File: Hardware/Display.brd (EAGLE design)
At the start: 48 x 70 mm, 54 parts, among them IC1 STM32F030C6T, IC2 VREG-TS1117CW-3V3, M1 WIRELESS-NRF24L01, Q1 BSS138, Q10 BSS138, Q11 IRLML5203, Q12 BSS138, Q13 IRLML5203, Q14 BSS138, Q15 IRLML5203, Q16 BSS138, Q2 BSS138, Q3 BSS138, Q4 BSS138, Q5 BSS138, Q6 BSS138, Q7 BSS138, Q8 BSS138, Q9 IRLML5203

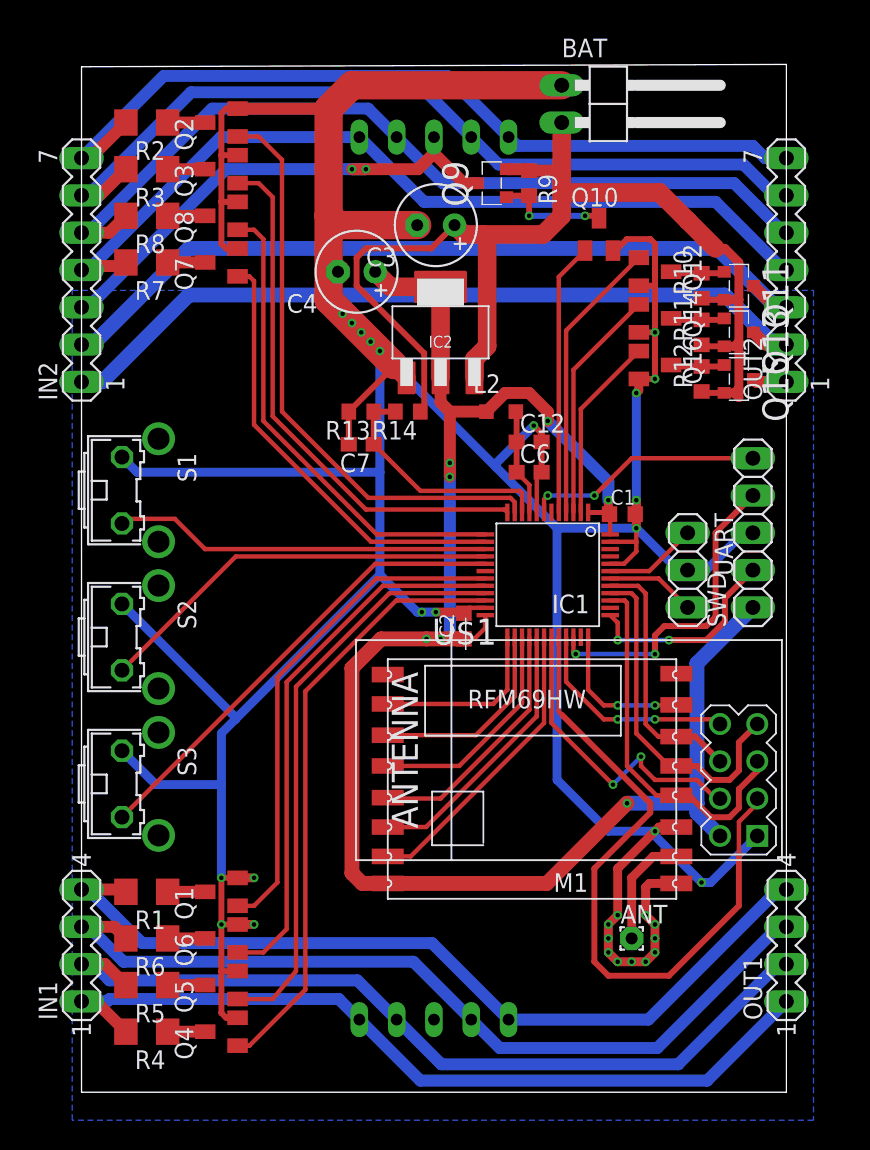
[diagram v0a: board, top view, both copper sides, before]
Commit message: Further software (Switches, HAL)
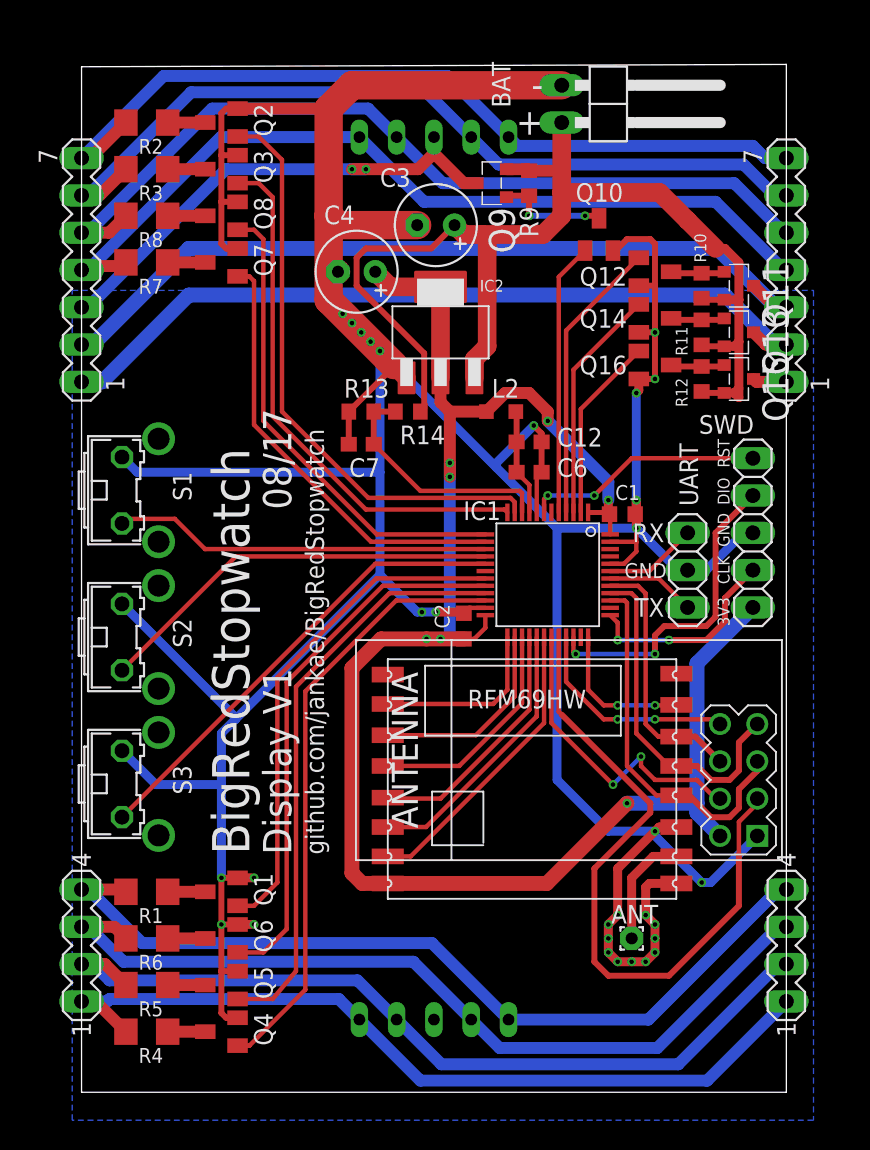
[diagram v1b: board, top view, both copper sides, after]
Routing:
- net GND: track 310.5 -> 312.4 mm
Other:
- board text added: "+"
- board text added: "-"
- board text added: "08/17"
- board text added: "3V3"
- board text added: "BigRedStopwatch"
- board text added: "CLK"
- board text added: "DIO"
- board text added: "Display V1"
- board text added: "GND"
- board text added: "RST"
- board text added: "RX"
- board text added: "TX"
- board text added: "github.com/jankae/BigRedStopwatch"

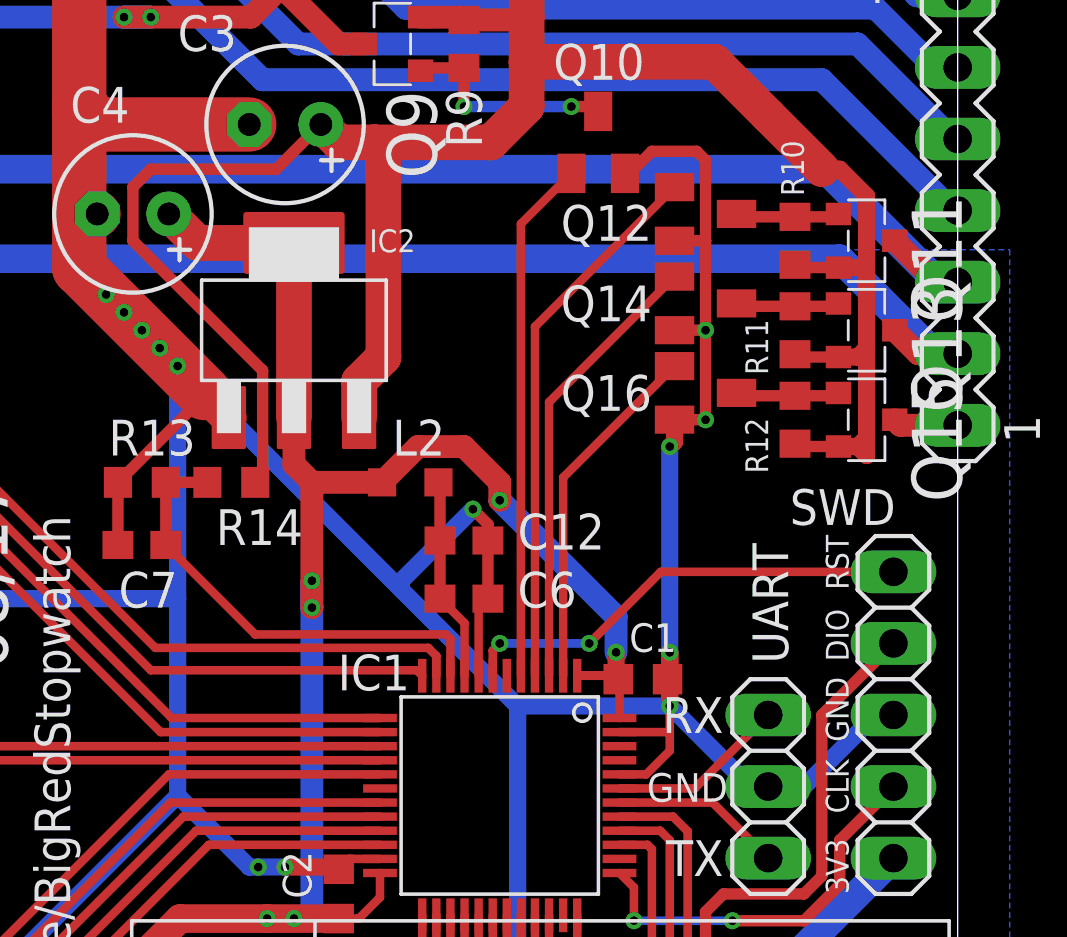
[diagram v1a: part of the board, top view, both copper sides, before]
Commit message: Added crystal to display board
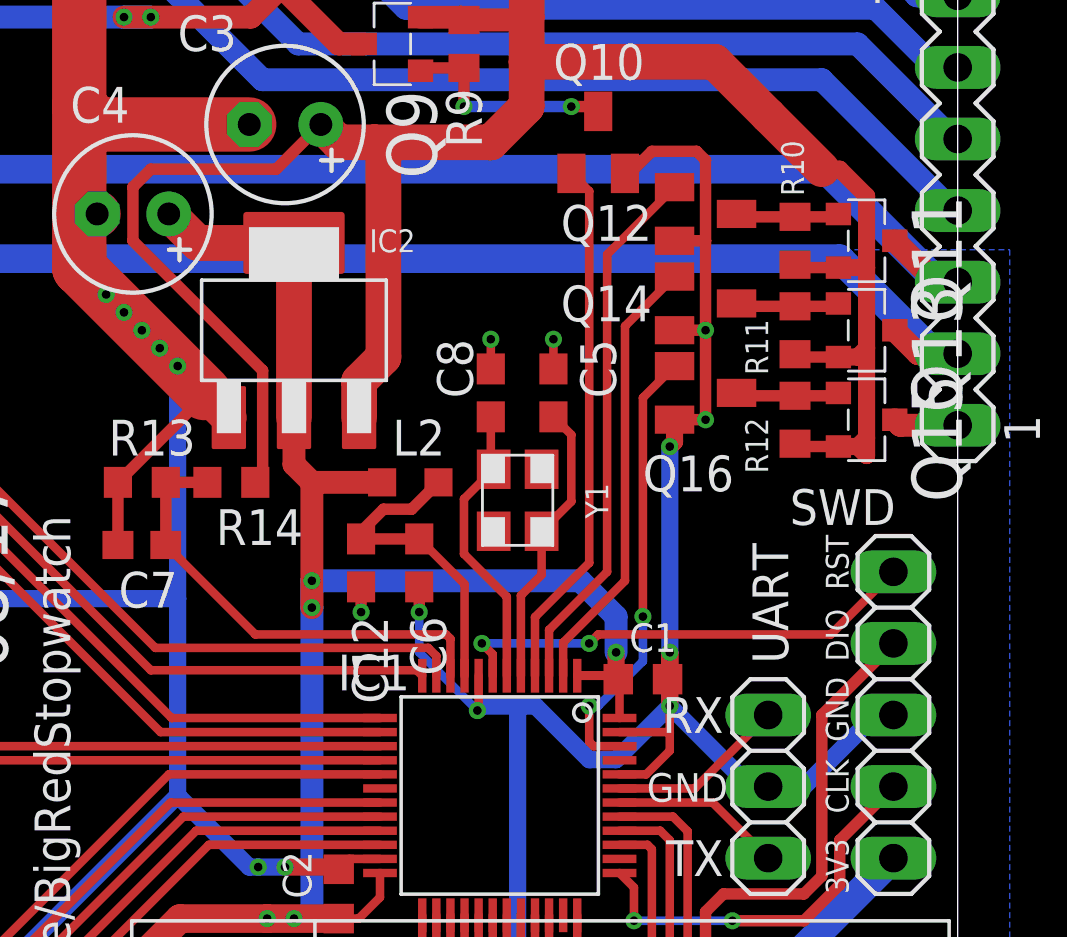
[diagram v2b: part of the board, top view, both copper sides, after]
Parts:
- added C5, C8: 12p, rcl:C0603
- added Y1: 8MHz, abracon:3.2X2.5MM
- moved C12 3.74 mm to (26.8, 43.5), turned to 270 degrees
- moved C6 2.03 mm to (28.9, 43.5), turned to 270 degrees
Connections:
- new net N$15: C5.2, IC1.5, Y1.3
- new net N$19: C8.2, IC1.6, Y1.1
- net DIGIT1: now also IC1.4; no longer IC1.5
- net DIGIT2: now also IC1.3; no longer IC1.4
- net DIGIT3: now also IC1.2; no longer IC1.3
- net DIGIT4: now also IC1.46; no longer IC1.2
- net GND: now also C5.1, C8.1
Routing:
- net GND: track 312.4 -> 297.7 mm, vias 30 -> 34
- net N$19: track 0.00 -> 10.3 mm
- net N$15: track 0.00 -> 10.2 mm
- net N$13: track 7.25 -> 11.4 mm
- net DIGIT4: track 12.6 -> 15.9 mm, vias 0 -> 2
- net NRST: track 16.3 -> 17.0 mm
- net +3V3: track 120.8 -> 120.4 mm, vias 7 -> 6
